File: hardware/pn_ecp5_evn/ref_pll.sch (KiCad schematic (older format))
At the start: 38 parts, among them J601 Conn_Coaxial, U601 LM2904, U602 OPA2211, X601 ABLNO

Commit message: first pass footprint assignment on pn r0
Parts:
- C601: value C_Small -> 1 nF; footprint (none) -> Capacitor_SMD:C_0402_1005Metric
- C602, C604, C605, C606, C607, C608, C609, C610: footprint (none) -> Capacitor_SMD:C_0402_1005Metric
- C603: value C_Small -> 1 uF; footprint (none) -> Capacitor_SMD:C_0402_1005Metric
- D601: value D_Small -> CDBU0340-HF; footprint (none) -> Diode_SMD:D_0603_1608Metric
- J601: footprint (none) -> Connector_Coaxial:U.FL_Hirose_U.FL-R-SMT-1_Vertical
- L601: value L_Small -> BLM15GG471; footprint (none) -> Inductor_SMD:L_0402_1005Metric
- R601, R602: value R_Small -> 51k; footprint (none) -> Resistor_SMD:R_0402_1005Metric
- R603, R606, R609, R610, R611, R612, R613, R614, R615, R616, R617: footprint (none) -> Resistor_SMD:R_0402_1005Metric
- R604, R605: value R_Small -> 1k; footprint (none) -> Resistor_SMD:R_0402_1005Metric
- R607, R608: value R_Small -> DNI; footprint (none) -> Resistor_SMD:R_0402_1005Metric
- TP601, TP602, TP603, TP604, TP605: footprint (none) -> TestPoint:TestPoint_Keystone_5015_Micro-Minature
- U601: footprint (none) -> Package_SO:MSOP-8_3x3mm_P0.65mm

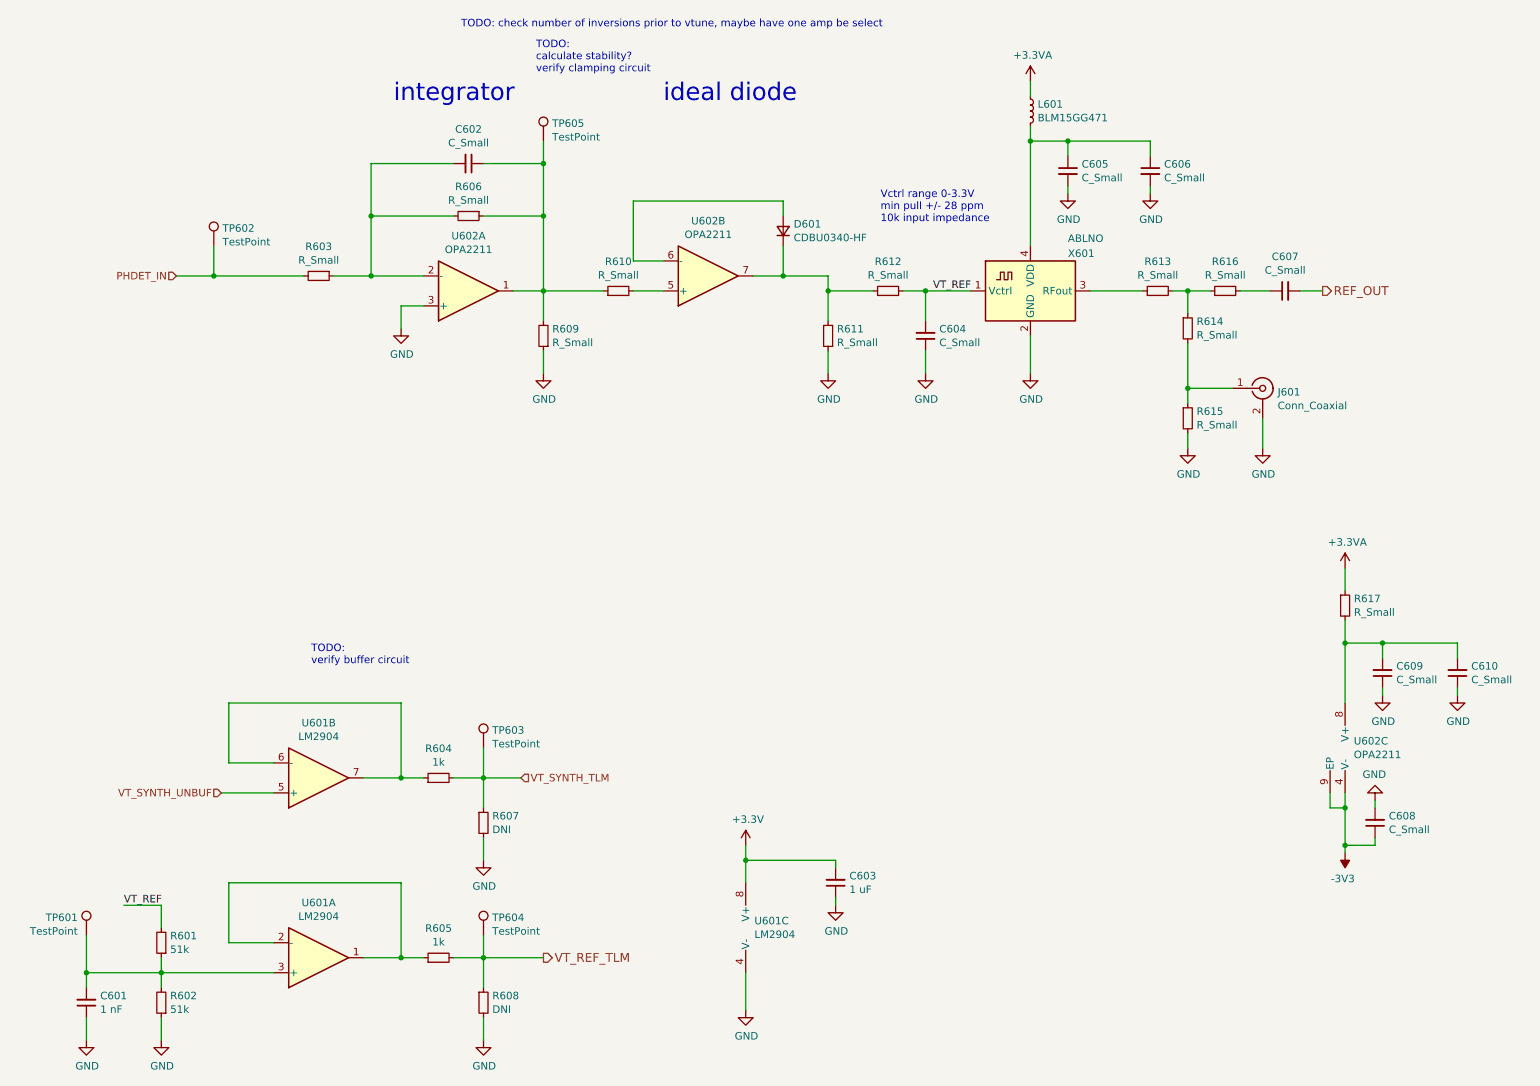
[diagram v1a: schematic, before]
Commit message: started component placement on phase noise analyzer
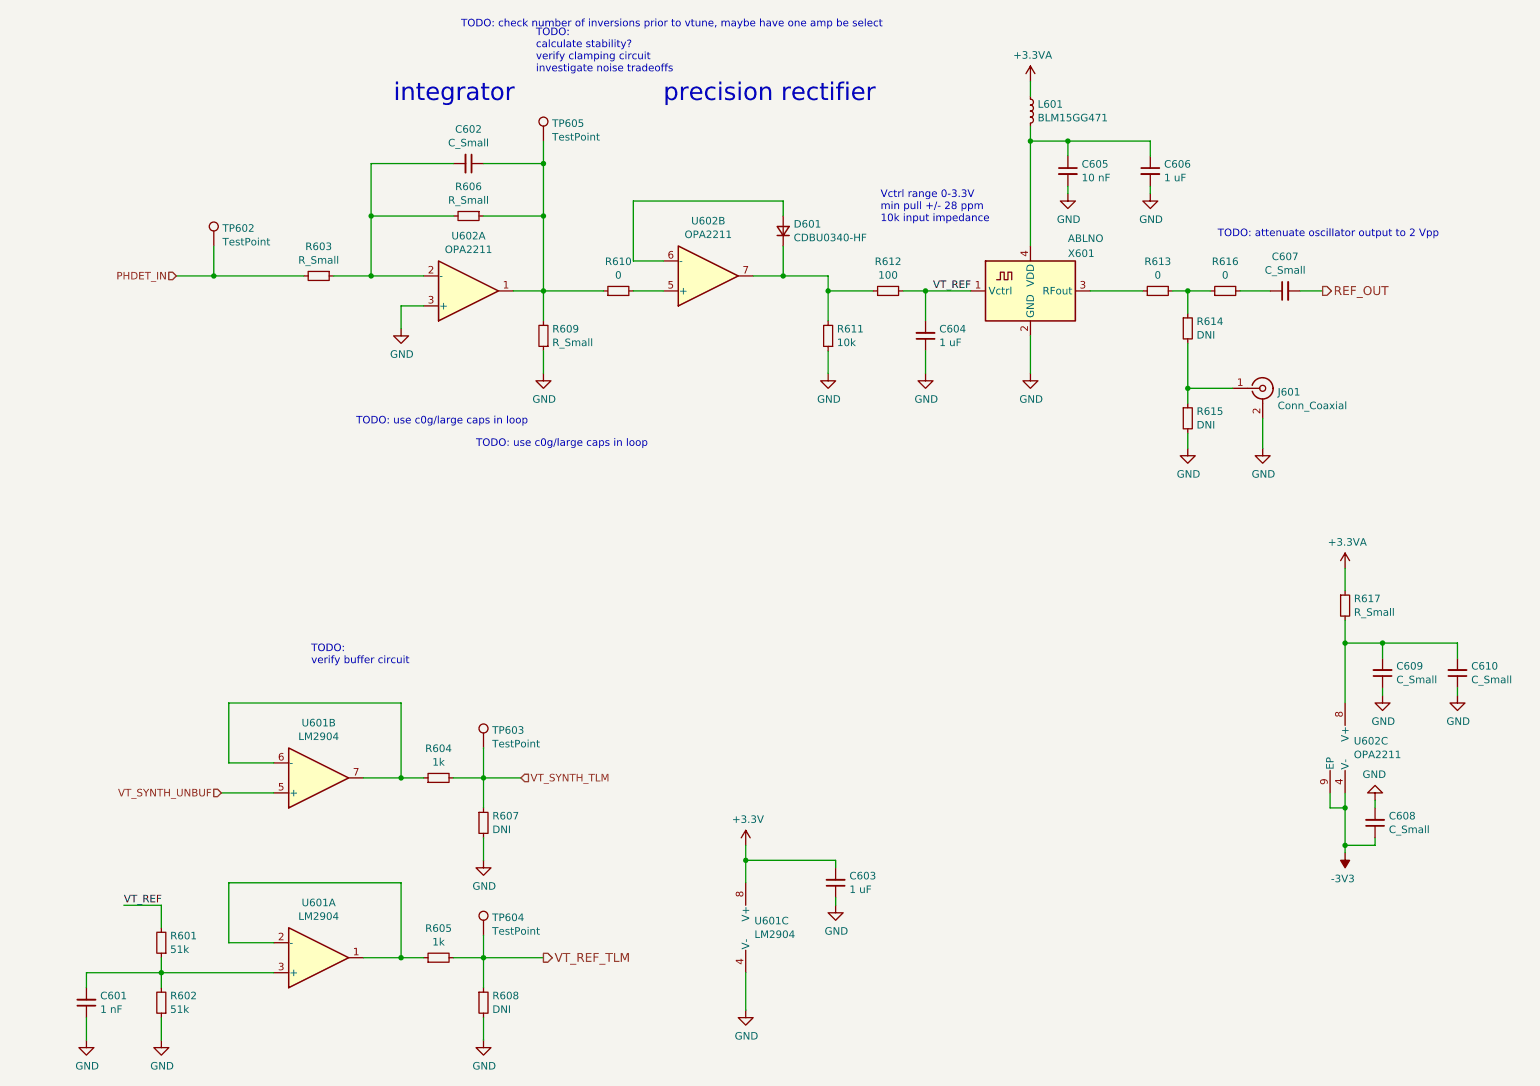
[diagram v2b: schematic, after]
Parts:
- removed TP601: TestPoint, TestPoint:TestPoint_Keystone_5015_Micro-Minature, symbol Connector:TestPoint
- C602: footprint Capacitor_SMD:C_0402_1005Metric -> Capacitor_SMD:C_0603_1608Metric
- C604: value C_Small -> 1 uF; footprint Capacitor_SMD:C_0402_1005Metric -> Capacitor_SMD:C_0603_1608Metric
- C605: value C_Small -> 10 nF
- C606: value C_Small -> 1 uF
- R610, R613, R616: value R_Small -> 0
- R611: value R_Small -> 10k
- R612: value R_Small -> 100
- R614, R615: value R_Small -> DNI
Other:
- note added: "TODO: attenuate oscillator output to 2 Vpp"
- note added: "TODO: use c0g/large caps in loop"
- note added: "TODO:\ncalculate stability?\nverify clamping circuit\ninvestigate noise tradeoffs"
- note added: "precision rectifier"
- note removed: "TODO:\ncalculate stability?\nverify clamping circuit"
- note removed: "ideal diode"
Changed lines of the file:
@@
 F 0 "C602" V 3421 1550 50  0000 C CNN
 F 1 "C_Small" V 3512 1550 50  0000 C CNN
-F 2 "Capacitor_SMD:C_0402_1005Metric" H 3650 1550 50  0001 C CNN
+F 2 "Capacitor_SMD:C_0603_1608Metric" H 3650 1550 50  0001 C CNN
 F 3 "~" H 3650 1550 50  0001 C CNN
 	1    3650 1550
@@
 AR Path="/5F4ECD93/5F4F2765" Ref="R612"  Part="1"
 F 0 "R612" V 6646 2400 50  0000 C CNN
-F 1 "R_Small" V 6555 2400 50  0000 C CNN
+F 1 "100" V 6555 2400 50  0000 C CNN
 F 2 "Resistor_SMD:R_0402_1005Metric" H 6450 2400 50  0001 C CNN
 F 3 "~" H 6450 2400 50  0001 C CNN
@@
 AR Path="/5F4ECD93/5F4F276B" Ref="C604"  Part="1"
 F 0 "C604" H 6608 2654 50  0000 R CNN
-F 1 "C_Small" H 6608 2745 50  0000 R CNN
-F 2 "Capacitor_SMD:C_0402_1005Metric" H 6700 2700 50  0001 C CNN
+F 1 "1 uF" H 6608 2745 50  0000 R CNN
+F 2 "Capacitor_SMD:C_0603_1608Metric" H 6700 2700 50  0001 C CNN
 F 3 "~" H 6700 2700 50  0001 C CNN
 	1    6700 2700
@@
 AR Path="/5F4ECD93/5F4F2784" Ref="C605"  Part="1"
 F 0 "C605" H 7742 1646 50  0000 L CNN
-F 1 "C_Small" H 7742 1555 50  0000 L CNN
+F 1 "10 nF" H 7742 1555 50  0000 L CNN
 F 2 "Capacitor_SMD:C_0402_1005Metric" H 7650 1600 50  0001 C CNN
 F 3 "~" H 7650 1600 50  0001 C CNN
@@
 AR Path="/5F4ECD93/5F4F278A" Ref="C606"  Part="1"
 F 0 "C606" H 8292 1646 50  0000 L CNN
-F 1 "C_Small" H 8292 1555 50  0000 L CNN
+F 1 "1 uF" H 8292 1555 50  0000 L CNN
 F 2 "Capacitor_SMD:C_0402_1005Metric" H 8200 1600 50  0001 C CNN
 F 3 "~" H 8200 1600 50  0001 C CNN
@@
 AR Path="/5F4ECD93/5F4F27C9" Ref="R610"  Part="1"
 F 0 "R610" V 4846 2400 50  0000 C CNN
-F 1 "R_Small" V 4755 2400 50  0000 C CNN
+F 1 "0" V 4755 2400 50  0000 C CNN
 F 2 "Resistor_SMD:R_0402_1005Metric" H 4650 2400 50  0001 C CNN
 F 3 "~" H 4650 2400 50  0001 C CNN
@@
 AR Path="/5F4ECD93/5F4F27DD" Ref="R611"  Part="1"
 F 0 "R611" H 5991 2654 50  0000 R CNN
-F 1 "R_Small" H 5991 2745 50  0000 R CNN
+F 1 "10k" H 5991 2745 50  0000 R CNN
 F 2 "Resistor_SMD:R_0402_1005Metric" H 6050 2700 50  0001 C CNN
 F 3 "~" H 6050 2700 50  0001 C CNN
@@
 AR Path="/5F4ECD93/5F6D0307" Ref="R613"  Part="1"
 F 0 "R613" V 8446 2400 50  0000 C CNN
-F 1 "R_Small" V 8355 2400 50  0000 C CNN
+F 1 "0" V 8355 2400 50  0000 C CNN
 F 2 "Resistor_SMD:R_0402_1005Metric" H 8250 2400 50  0001 C CNN
 F 3 "~" H 8250 2400 50  0001 C CNN
@@
 AR Path="/5F4ECD93/5F6DDC7F" Ref="R616"  Part="1"
 F 0 "R616" V 8896 2400 50  0000 C CNN
-F 1 "R_Small" V 8805 2400 50  0000 C CNN
+F 1 "0" V 8805 2400 50  0000 C CNN
 F 2 "Resistor_SMD:R_0402_1005Metric" H 8700 2400 50  0001 C CNN
 F 3 "~" H 8700 2400 50  0001 C CNN
@@
 AR Path="/5F4ECD93/5F6DE0EC" Ref="R614"  Part="1"
 F 0 "R614" H 8509 2696 50  0000 L CNN
-F 1 "R_Small" H 8509 2605 50  0000 L CNN
+F 1 "DNI" H 8509 2605 50  0000 L CNN
 F 2 "Resistor_SMD:R_0402_1005Metric" H 8450 2650 50  0001 C CNN
 F 3 "~" H 8450 2650 50  0001 C CNN
@@
 AR Path="/5F4ECD93/5F6ED4C4" Ref="R615"  Part="1"
 F 0 "R615" H 8509 3296 50  0000 L CNN
-F 1 "R_Small" H 8509 3205 50  0000 L CNN
+F 1 "DNI" H 8509 3205 50  0000 L CNN
 F 2 "Resistor_SMD:R_0402_1005Metric" H 8450 3250 50  0001 C CNN
 F 3 "~" H 8450 3250 50  0001 C CNN
@@
 	8800 2400 9000 2400
 $Comp
-L Connector:TestPoint TP601
-U 1 1 5F71DFF3
-P 1100 6700
-F 0 "TP601" H 1158 6818 50  0000 L CNN
-F 1 "TestPoint" H 1158 6727 50  0000 L CNN
-F 2 "TestPoint:TestPoint_Keystone_5015_Micro-Minature" H 1300 6700 50  0001 C CNN
-F 3 "~" H 1300 6700 50  0001 C CNN
-	1    1100 6700
-	-1   0    0    -1
-$EndComp
-$Comp
 L Connector:TestPoint TP605
 U 1 1 5F7225E6
@@
 	3750 6700 3750 6850
 Wire Wire Line
-	1100 6700 1100 6950
-Connection ~ 1100 6950
-Wire Wire Line
 	1950 2300 1700 2300
 Connection ~ 1950 2300
@@
 PHDET_IN
 Text Notes 4100 950  0    50   ~ 0
-TODO:\ncalculate stability?\nverify clamping circuit
+TODO:\ncalculate stability?\nverify clamping circuit\ninvestigate noise tradeoffs
 Text Notes 2600 4900 0    50   ~ 0
 TODO:\nverify buffer circuit
@@
 integrator
 Text Notes 4950 1150 0    118  ~ 0
-ideal diode
+precision rectifier
+Text Notes 3700 3450 0    50   ~ 0
+TODO: use c0g/large caps in loop
+Text Notes 8650 2050 0    50   ~ 0
+TODO: attenuate oscillator output to 2 Vpp
+Text Notes 2900 3300 0    50   ~ 0
+TODO: use c0g/large caps in loop
 $EndSCHEMATC

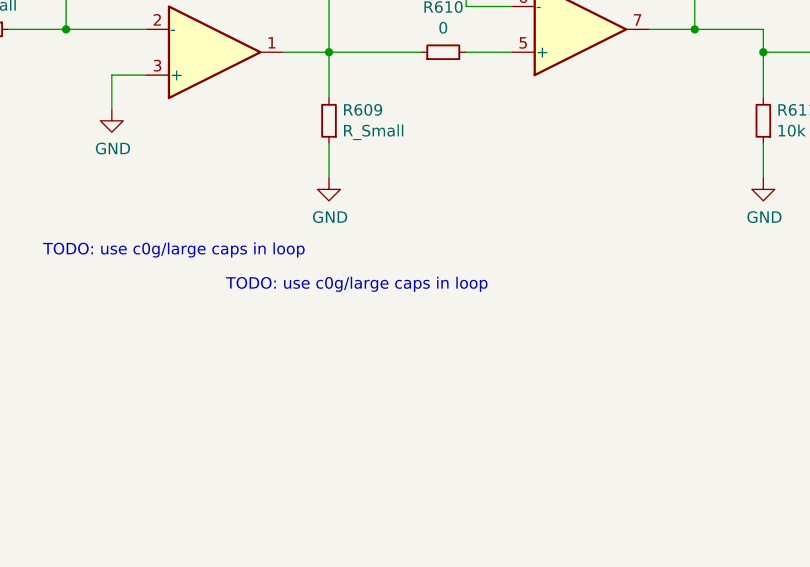
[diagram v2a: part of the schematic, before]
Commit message: work on routing phase noise downconverter
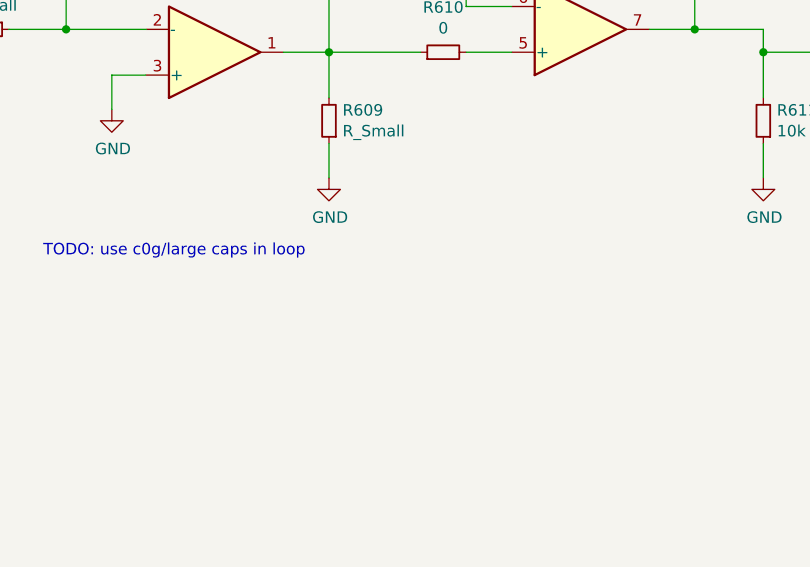
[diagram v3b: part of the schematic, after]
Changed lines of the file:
@@
 Text Notes 4950 1150 0    118  ~ 0
 precision rectifier
-Text Notes 3700 3450 0    50   ~ 0
-TODO: use c0g/large caps in loop
 Text Notes 8650 2050 0    50   ~ 0
 TODO: attenuate oscillator output to 2 Vpp

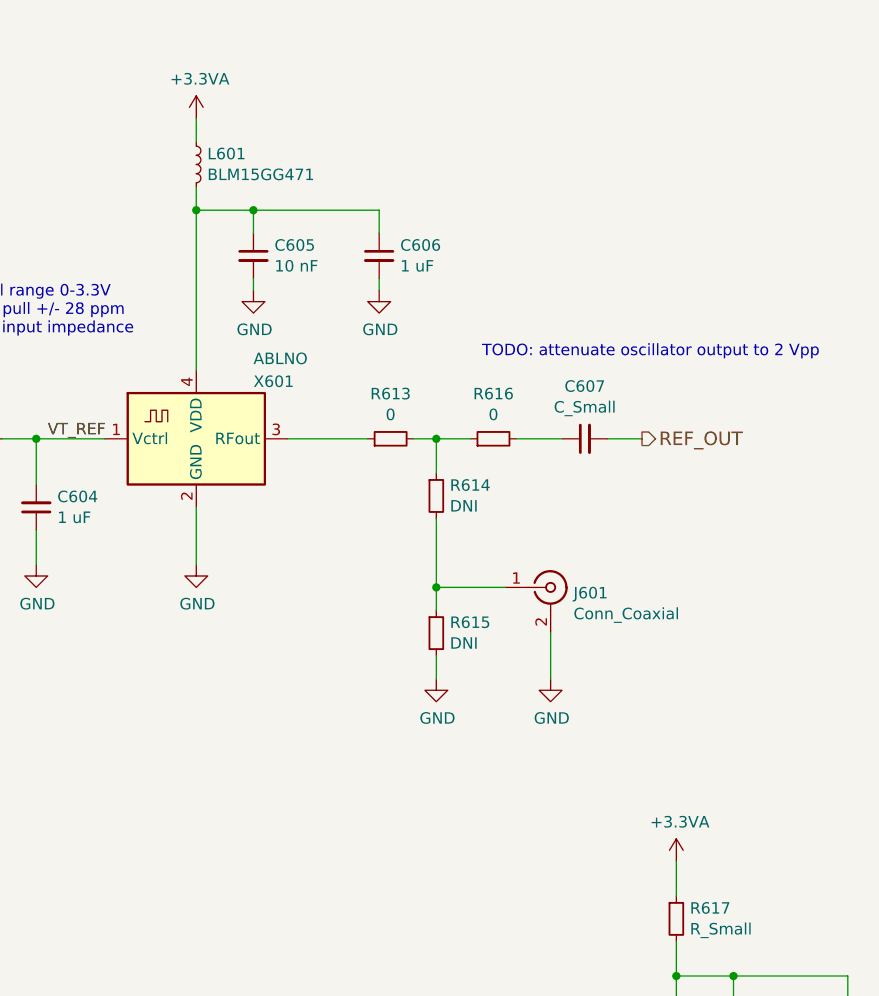
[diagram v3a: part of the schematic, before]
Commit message: layout of phase noise downconverter
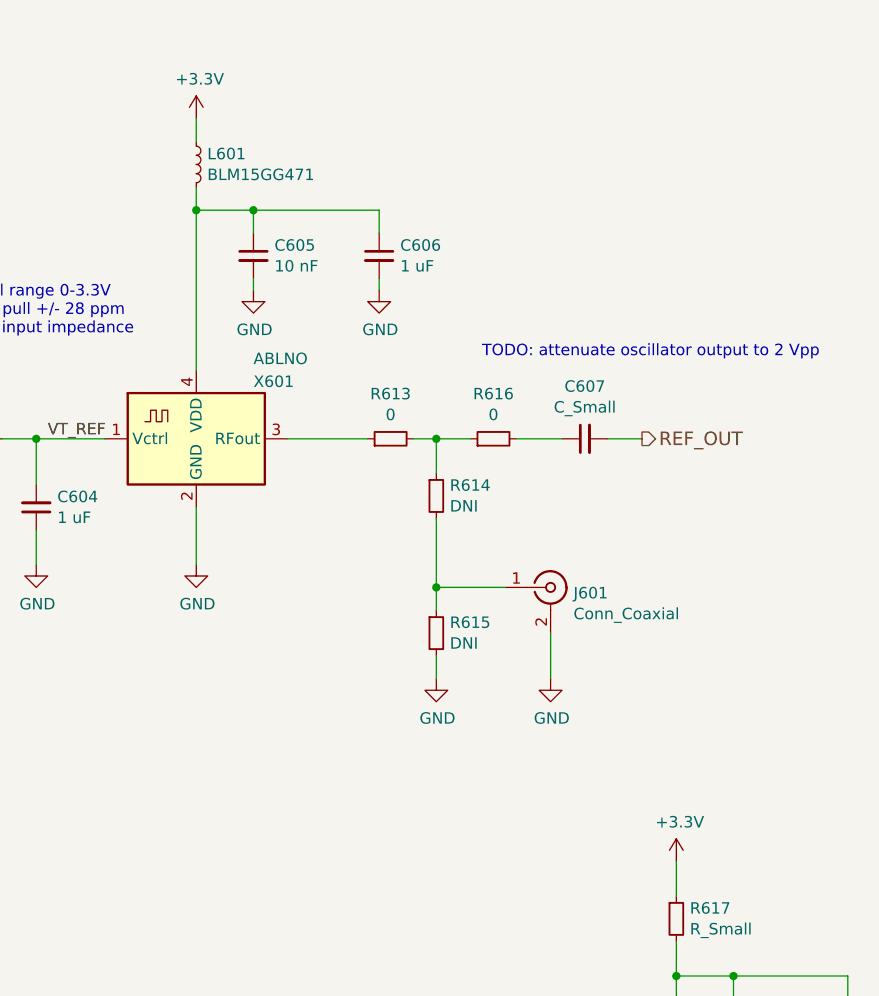
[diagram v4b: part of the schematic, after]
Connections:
- net +3.3VA is gone; now on net +3V3: L601.1, R617.1
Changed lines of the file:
@@
 Comment4 ""
 $EndDescr
-$Comp
-L power:+3.3VA #PWR?
-U 1 1 5F4F26F5
-P 7400 1000
-AR Path="/5F265927/5F4F26F5" Ref="#PWR?"  Part="1"
-AR Path="/5F4ECD93/5F4F26F5" Ref="#PWR0197"  Part="1"
-F 0 "#PWR0197" H 7400 850 50  0001 C CNN
-F 1 "+3.3VA" H 7415 1173 50  0000 C CNN
-F 2 "" H 7400 1000 50  0001 C CNN
-F 3 "" H 7400 1000 50  0001 C CNN
-	1    7400 1000
-	1    0    0    -1
-$EndComp
 Wire Wire Line
 	1100 6950 1100 7050
@@
 Wire Wire Line
 	9500 4250 9500 4400
-$Comp
-L power:+3.3VA #PWR?
-U 1 1 5F4F27EA
-P 9500 4250
-AR Path="/5F265927/5F4F27EA" Ref="#PWR?"  Part="1"
-AR Path="/5F4ECD93/5F4F27EA" Ref="#PWR0207"  Part="1"
-F 0 "#PWR0207" H 9500 4100 50  0001 C CNN
-F 1 "+3.3VA" H 9515 4423 50  0000 C CNN
-F 2 "" H 9500 4250 50  0001 C CNN
-F 3 "" H 9500 4250 50  0001 C CNN
-	1    9500 4250
-	1    0    0    -1
-$EndComp
 Connection ~ 9750 4750
 Wire Wire Line
@@
 Text Notes 2900 3300 0    50   ~ 0
 TODO: use c0g/large caps in loop
+$Comp
+L power:+3.3V #PWR0197
+U 1 1 5F4A19B2
+P 7400 1000
+F 0 "#PWR0197" H 7400 850 50  0001 C CNN
+F 1 "+3.3V" H 7415 1173 50  0000 C CNN
+F 2 "" H 7400 1000 50  0001 C CNN
+F 3 "" H 7400 1000 50  0001 C CNN
+	1    7400 1000
+	1    0    0    -1
+$EndComp
+$Comp
+L power:+3.3V #PWR0207
+U 1 1 5F4A1D60
+P 9500 4250
+F 0 "#PWR0207" H 9500 4100 50  0001 C CNN
+F 1 "+3.3V" H 9515 4423 50  0000 C CNN
+F 2 "" H 9500 4250 50  0001 C CNN
+F 3 "" H 9500 4250 50  0001 C CNN
+	1    9500 4250
+	1    0    0    -1
+$EndComp
 $EndSCHEMATC
